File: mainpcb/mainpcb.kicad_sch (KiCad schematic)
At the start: 22 parts, among them J1 Raspberry_Pi_2_3, J13 Screw_Terminal_01x08, J15 Screw_Terminal_01x02, J2 8P8C_Shielded, J3 8P8C_Shielded, J4 Screw_Terminal_01x08, J9 Screw_Terminal_01x02, U1 TCA9509DGKR, U2 TXB0108PW

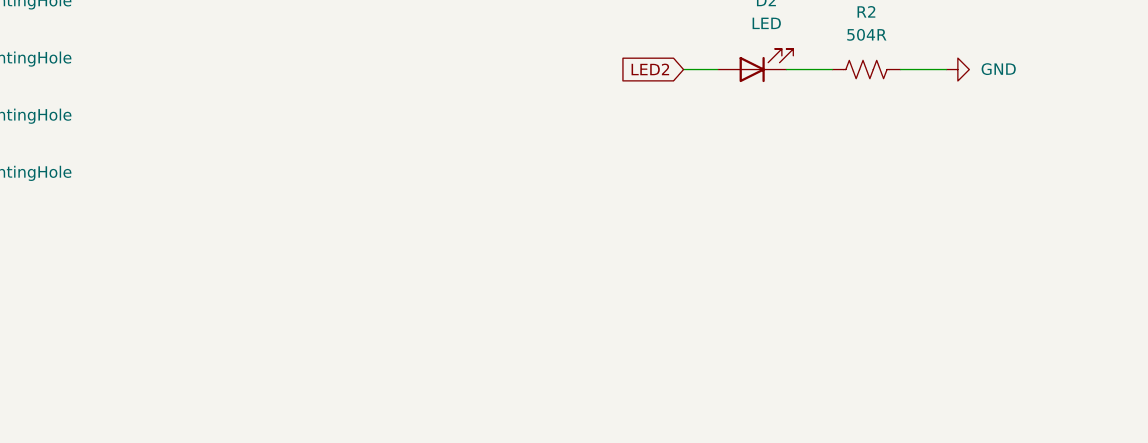
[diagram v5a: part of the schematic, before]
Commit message: Added drawing information boxes
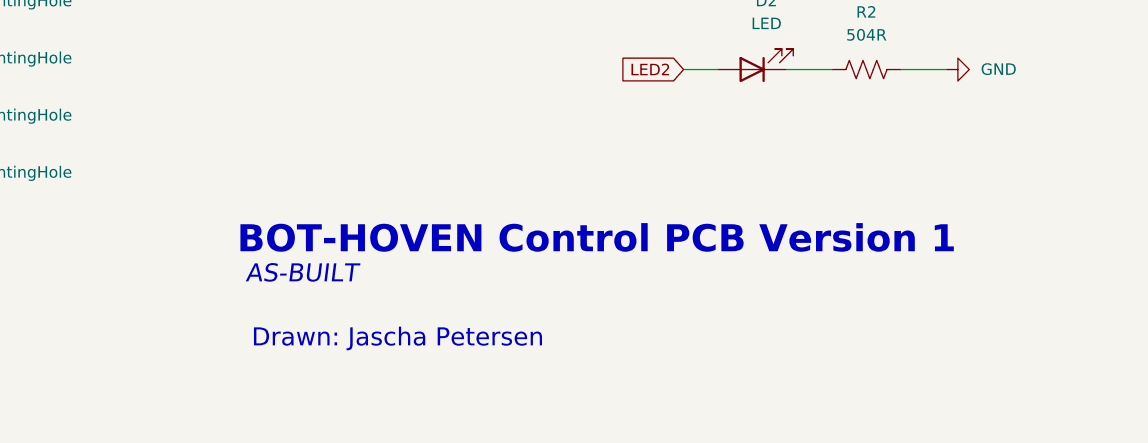
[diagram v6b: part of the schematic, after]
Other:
- note added: "AS-BUILT"
- note added: "BOT-HOVEN Control PCB Version 1"
- note added: "Drawn: Jascha Petersen"
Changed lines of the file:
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@@
+		)
+	)
+	(text "BOT-HOVEN Control PCB Version 1"
+		(exclude_from_sim no)
+		(at 217.678 168.91 0)
+		(effects
+			(font
+				(size 3 3)
+				(thickness 0.6)
+				(bold yes)
+			)
 		)
 	)
@@
 			)
 		)
+	)
+	(text "AS-BUILT"
+		(exclude_from_sim no)
+		(at 184.912 172.72 0)
+		(effects
+			(font
+				(size 2 2)
+				(italic yes)
+			)
+		)
+	)
+	(text "Drawn: Jascha Petersen"
+		(exclude_from_sim no)
+		(at 195.58 179.832 0)
+		(effects
+			(font
+				(size 2 2)
+			)
+		)

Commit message: Added PDF schematic exports
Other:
- title: (none) -> Control PCB Main
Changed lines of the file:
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@@
 	(generator_version "8.0")
 	(paper "A4")
+	(title_block
+		(title "Control PCB Main")
+	)
 	(junction
 		(at 38.1 175.26)
